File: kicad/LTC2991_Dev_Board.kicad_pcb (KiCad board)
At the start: 2 copper layers, 46.2 x 38.4 mm, 17 parts, among them P1 CONN_01X07, P2 CONN_01X07, Q1 MMBT3904, Q2 MMBT3904, Q3 MMBT3904, Q4 MMBT3904, SW1 DIP-SPDT-3, U1 LTC2991

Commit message: More PCB layout work, schematic tweaks. Closer to a finaly layout.
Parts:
- removed REF**: DIP_switch_2x06, Local:DIP_Switch_2x06
- removed REF**: Pin_Header_Straight_2x03, Pin_Headers:Pin_Header_Straight_2x03
- removed SW1: DIP-SPDT-3, Local:DIP_Switch_2x06
- added P3: CONN_02X03, Pin_Headers:Pin_Header_Straight_2x03, F.Cu at (99.8, 100.3)
- R1, R2, R3, R4: footprint Resistors_SMD:R_2010 -> Resistors_SMD:R_1206
- R5, R6, R7: footprint Resistors_SMD:R_1206 -> Resistors_SMD:R_0603
- moved R7 38.3 mm to (104.9, 92.3), turned to 270 degrees
- moved R6 33.8 mm to (102.4, 92.3), turned to 270 degrees
- moved R5 29.8 mm to (99.8, 92.3), turned to 270 degrees
- moved Q3 13.4 mm to (113.3, 100.2), turned to 180 degrees
- moved Q4 9.79 mm to (113.3, 90.6), turned to 180 degrees
- moved U1 7.37 mm to (102.4, 85.1)
- moved Q2 7.24 mm to (91.3, 100.2), turned to 180 degrees
- moved Q1 7.00 mm to (91.3, 90.6), turned to 180 degrees
- moved R4 1.49 mm to (113.3, 87.2), turned to 0 degrees
- moved R1 1.45 mm to (91.3, 87.2), turned to 0 degrees
- moved R3 0.81 mm to (113.3, 96.9), turned to 0 degrees
- moved R2 0.74 mm to (91.3, 96.9), turned to 0 degrees
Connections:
- R5 pad 2: Net-(R5-Pad2) -> Net-(P3-Pad2)
- R6 pad 2: Net-(R6-Pad2) -> Net-(P3-Pad4)
- R7 pad 2: Net-(R7-Pad2) -> Net-(P3-Pad6)
- U1 pad 13: Net-(SW1-Pad5) -> Net-(P3-Pad6)
- U1 pad 14: Net-(SW1-Pad3) -> Net-(P3-Pad4)
- U1 pad 15: Net-(SW1-Pad1) -> Net-(P3-Pad2)
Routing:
- net Net-(P3-Pad2): track 0.00 -> 18.2 mm, vias 0 -> 2
- net Net-(P3-Pad4): track 0.00 -> 17.2 mm, vias 0 -> 2
- net /V1: track 25.7 -> 9.36 mm
- net Net-(P3-Pad6): track 0.00 -> 16.2 mm
- net /V3: track 22.3 -> 8.14 mm
- net /VCC: track 0.00 -> 14.2 mm
- net /V5: track 5.12 -> 14.1 mm
- net /V7: track 7.94 -> 13.9 mm
- net /V2: track 17.3 -> 13.5 mm
- net /V6: track 7.23 -> 9.51 mm
- net /V4: track 14.4 -> 12.6 mm
- added copper zone on F.Cu, net /GND
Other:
- board size 46.2 x 38.4 mm -> 29.5 x 22 mm
- net class Default: trace_width 0.3048 -> 0.254; via_dia 0.6 -> 0.508; via_drill 0.4 -> 0.3302
- net class Power: clearance 0.3048 -> 0.2032; via_dia 0.6 -> 0.762; via_drill 0.4 -> 0.508
- rule trace_min: 0.2 -> 0.1524
- rule via_min_drill: 0.3 -> 0.3302
- rule via_min_size: 0.4 -> 0.508

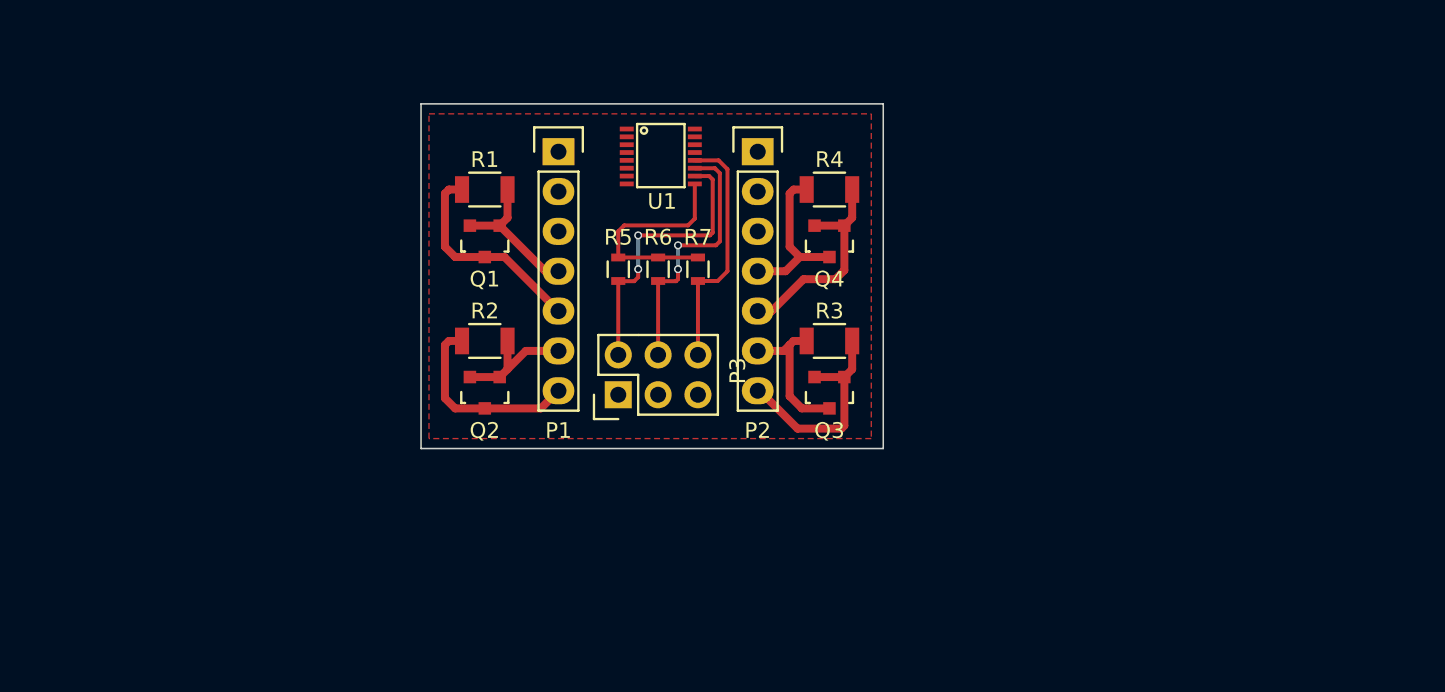
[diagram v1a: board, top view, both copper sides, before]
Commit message: Final schematic and PCB layout for Rev. A. Significantly simplified the schematic in order to make the board as compact as possible.
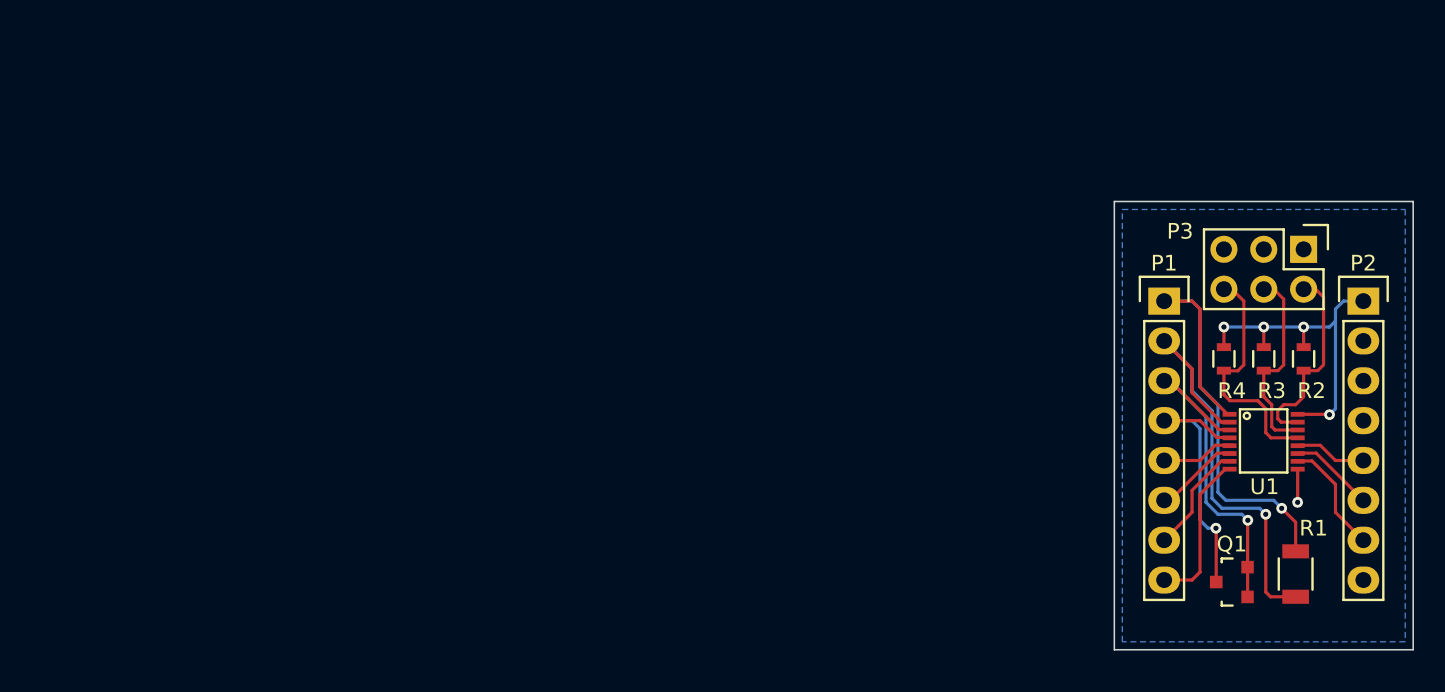
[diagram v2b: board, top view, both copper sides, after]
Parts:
- removed Q2, Q3, Q4: MMBT3904, Housings_SOT-23_SOT-143_TSOT-6:SOT-23
- removed R5, R6, R7: 5k6, Resistors_SMD:R_0603
- P1, P2: value CONN_01X07 -> CONN_01X08; footprint Pin_Headers:Pin_Header_Straight_1x07 -> Pin_Headers:Pin_Header_Straight_1x08
- R2, R3, R4: value 0.1 -> 5k6; footprint Resistors_SMD:R_1206 -> Resistors_SMD:R_0603
- moved R1 57.2 mm to (143.0, 111.8), turned to 90 degrees
- moved Q1 52.3 mm to (138.9, 112.3), turned to 90 degrees
- moved R2 52.2 mm to (143.5, 98.0), turned to 270 degrees
- moved P3 44.7 mm to (143.5, 91.1), turned to 270 degrees
- moved U1 42.7 mm to (141.0, 103.3)
- moved P1 39.8 mm to (134.6, 94.4)
- moved P2 39.8 mm to (147.3, 94.4)
- moved R3 27.7 mm to (141.0, 98.0), turned to 270 degrees
- moved R4 27.4 mm to (138.4, 98.0), turned to 270 degrees
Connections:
- P1 pad 1: /VCC -> /V1
- P1 pad 2: /SCL -> /V2
- P1 pad 3: /SDA -> /V3
- P1 pad 4: /V1 -> /V4
- P1 pad 5: /V2 -> /V5
- P1 pad 6: /V3 -> /V6
- P1 pad 7: /V4 -> /V7
- P2 pad 1: /GND -> /VCC
- P2 pad 2: /PWM -> /GND
- P2 pad 4: /V8 -> /GND
- P2 pad 5: /V7 -> /PWM
- P2 pad 6: /V6 -> /SCL
- P2 pad 7: /V5 -> /SDA
- Q1 pad 1: /V1 -> /V3
- Q1 pad 2: /V1 -> /V3
- Q1 pad 3: /V2 -> /V4
- R2 pad 1: /V4 -> /VCC
- R2 pad 2: /V3 -> Net-(P3-Pad2)
- R3 pad 1: /V6 -> /VCC
- R3 pad 2: /V5 -> Net-(P3-Pad4)
- R4 pad 1: /V8 -> /VCC
- R4 pad 2: /V7 -> Net-(P3-Pad6)
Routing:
- net /V1: track 9.36 -> 32.3 mm, vias 0 -> 1
- net /V2: track 13.5 -> 29.3 mm, vias 0 -> 1
- net /V3: track 8.14 -> 22.4 mm, vias 0 -> 1
- net /V5: track 14.1 -> 4.75 mm
- net /VCC: track 14.2 -> 22.0 mm, vias 0 -> 4
- net /SDA: track 0.00 -> 7.14 mm
- net /V7: track 13.9 -> 7.26 mm
- net Net-(P3-Pad2): track 18.2 -> 12.8 mm, vias 2 -> 0
- net /SCL: track 0.00 -> 5.26 mm
- net /V4: track 12.6 -> 17.8 mm, vias 0 -> 1
- net Net-(P3-Pad4): track 17.2 -> 12.7 mm, vias 2 -> 0
- net /PWM: track 0.00 -> 4.41 mm
- net /V6: track 9.51 -> 5.60 mm
- net /GND: track 0.46 -> 2.11 mm, vias 0 -> 1
- net Net-(P3-Pad6): track 16.2 -> 15.4 mm
- added copper zone on B.Cu, net /GND
- removed copper zone on F.Cu, net /GND
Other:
- board size 29.5 x 22 mm -> 19.1 x 28.6 mm
- net class Default: clearance 0.2032 -> 0.1524; trace_width 0.254 -> 0.2032; via_dia 0.508 -> 0.6858
- net class Power removed
- rule trace_clearance: 0.2032 -> 0.1524
- rule via_min_size: 0.508 -> 0.6858
- board text added: "LTC2991 Dev Board Rev. A, July 2015 http://www.nellump.net/"

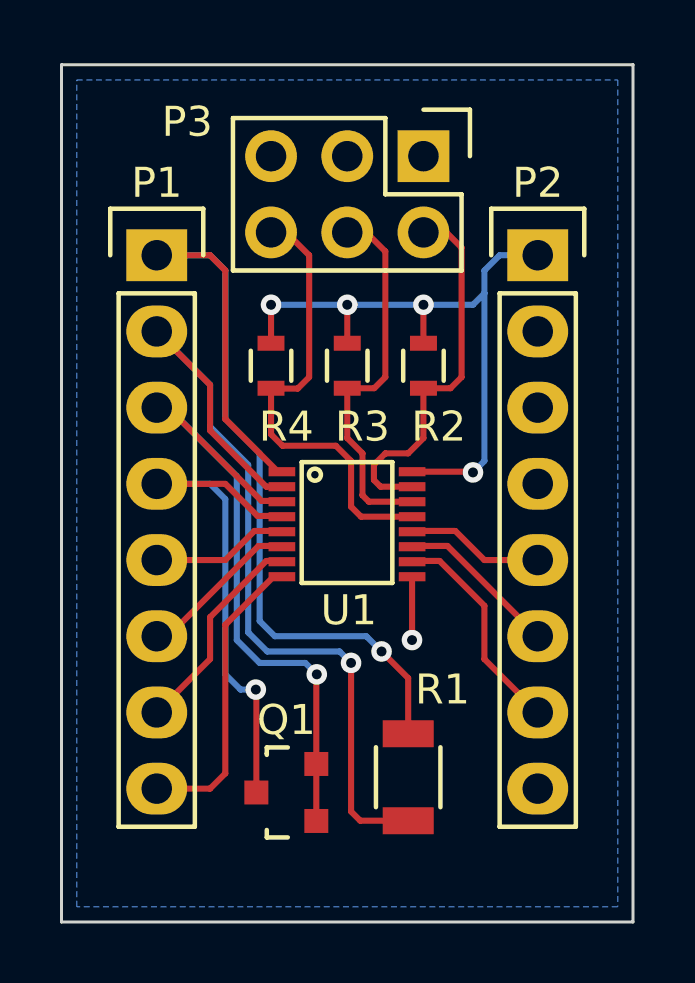
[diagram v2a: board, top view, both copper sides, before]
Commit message: Minor adjustment to PCB silkscreen. Added labels to pins in address jumper. Moved board name to front side.
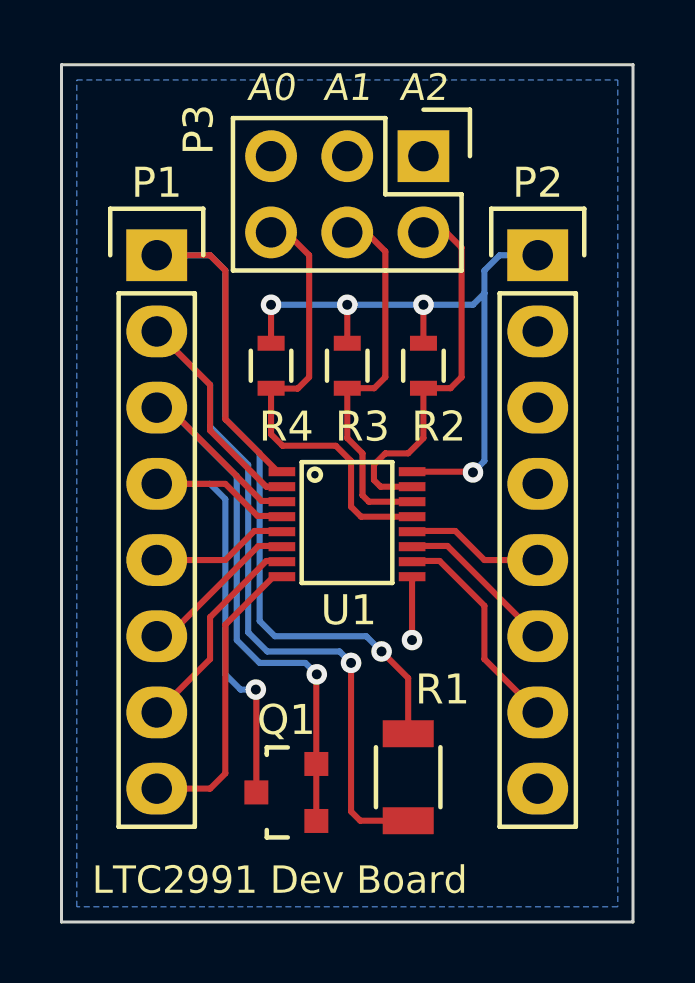
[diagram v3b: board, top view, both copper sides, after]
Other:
- board text added: "A0"
- board text added: "A1"
- board text added: "A2"
- board text added: "LTC2991 Dev Board"
- board text added: "Rev. A, July 2015 http://www.nellump.net/"
- board text removed: "LTC2991 Dev Board Rev. A, July 2015 http://www.nellump.net/"
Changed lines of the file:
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@@
     (links 33)
     (no_connects 0)
-    (area 129.559267 87.960999 152.380734 116.636001)
+    (area 129.559267 87.9221 152.380734 116.636001)
     (thickness 1.6)
-    (drawings 5)
+    (drawings 9)
     (tracks 135)
     (zones 0)
@@
     (descr "Through hole pin header")
     (tags "pin header")
-    (fp_text reference P3 (at -1.143 7.874 360) (layer F.SilkS)
+    (fp_text reference P3 (at -0.889 7.493 450) (layer F.SilkS)
       (effects (font (size 1 1) (thickness 0.15)))
     )
@@
       (net 1 /VCC))
   )
-  (gr_text "LTC2991 Dev Board\nRev. A, July 2015\nhttp://www.nellump.net/" (at 140.97 96.774 90) (layer B.SilkS)
+  (gr_text "LTC2991 Dev Board" (at 132.461 115.189) (layer F.SilkS)
+    (effects (font (size 0.9144 0.9144) (thickness 0.1524)) (justify left))
+  )
+  (gr_text A2 (at 143.51 88.773) (layer F.SilkS)
+    (effects (font (size 0.889 0.889) (thickness 0.1524) italic))
+  )
+  (gr_text A1 (at 140.97 88.773) (layer F.SilkS)
+    (effects (font (size 0.889 0.889) (thickness 0.1524) italic))
+  )
+  (gr_text A0 (at 138.43 88.773) (layer F.SilkS)
+    (effects (font (size 0.889 0.889) (thickness 0.1524) italic))
+  )
+  (gr_text "Rev. A, July 2015\nhttp://www.nellump.net/" (at 140.97 96.139 90) (layer B.SilkS)
     (effects (font (size 1.016 1.016) (thickness 0.254)) (justify left mirror))
   )

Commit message: Minor adjustments to text on PCB's back silkscreen.
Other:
- board text added: "Rev. A, July 2015 http://www.nellump.net/ltcdev"
- board text removed: "Rev. A, July 2015 http://www.nellump.net/"
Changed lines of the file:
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@@
   (title_block
     (title "LTC2991 Development Board")
-    (date 2015-07-15)
+    (date 2015-07-17)
     (rev A)
     (company "Paul Mullen <pm@nellump.net>")
@@
     (visible_elements FFFFF77F)
     (pcbplotparams
-      (layerselection 0x010f0_80000001)
+      (layerselection 0x010f8_80000001)
       (usegerberextensions false)
       (excludeedgelayer true)
@@
       (drillshape 0)
       (scaleselection 1)
-      (outputdirectory ""))
+      (outputdirectory ../gerbers/))
   )
   (net 0 "")
@@
     (effects (font (size 0.889 0.889) (thickness 0.1524) italic))
   )
-  (gr_text "Rev. A, July 2015\nhttp://www.nellump.net/" (at 140.97 96.139 90) (layer B.SilkS)
-    (effects (font (size 1.016 1.016) (thickness 0.254)) (justify left mirror))
+  (gr_text "Rev. A, July 2015\nhttp://www.nellump.net/ltcdev" (at 140.97 94.996 90) (layer B.SilkS)
+    (effects (font (size 1.016 0.889) (thickness 0.1905)) (justify left mirror))
   )
   (gr_line (start 131.445 116.586) (end 131.445 88.011) (angle 90) (layer Edge.Cuts) (width 0.1))

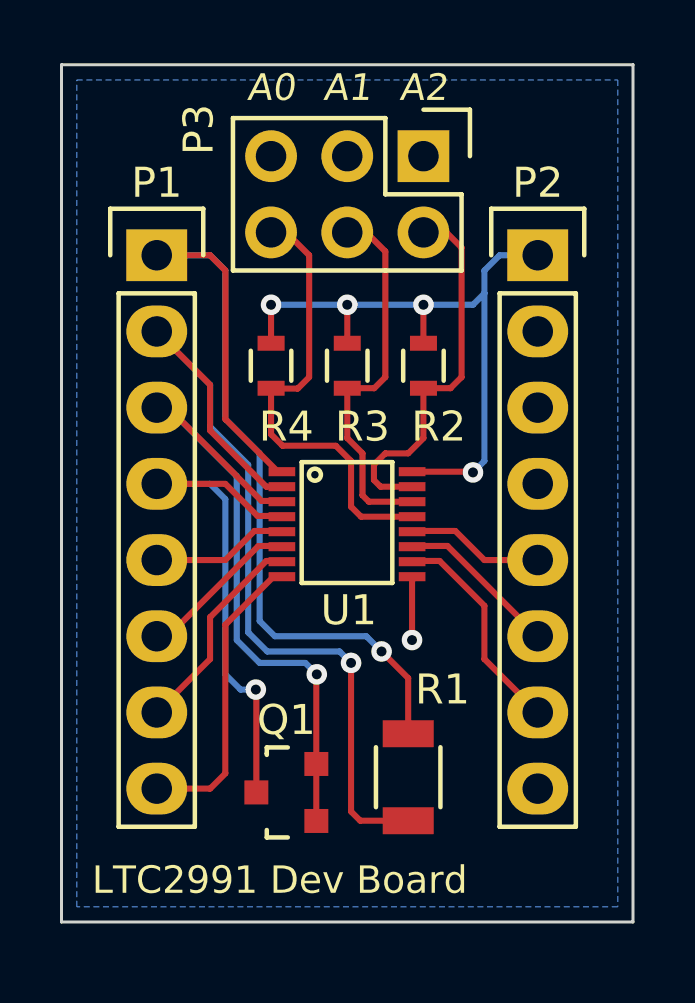
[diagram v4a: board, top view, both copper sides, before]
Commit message: Modified schematic and PCB layout. 1. Added two-pin header for measurement of external current source via    on-board shunt resistor (both optional). 2. Added filter capacitor for IC power. 3. Added filter capacitor for temperature-sensing transistor (both    optional). 4. Placed noise-shielding traces around temperature-sensing    transistor.
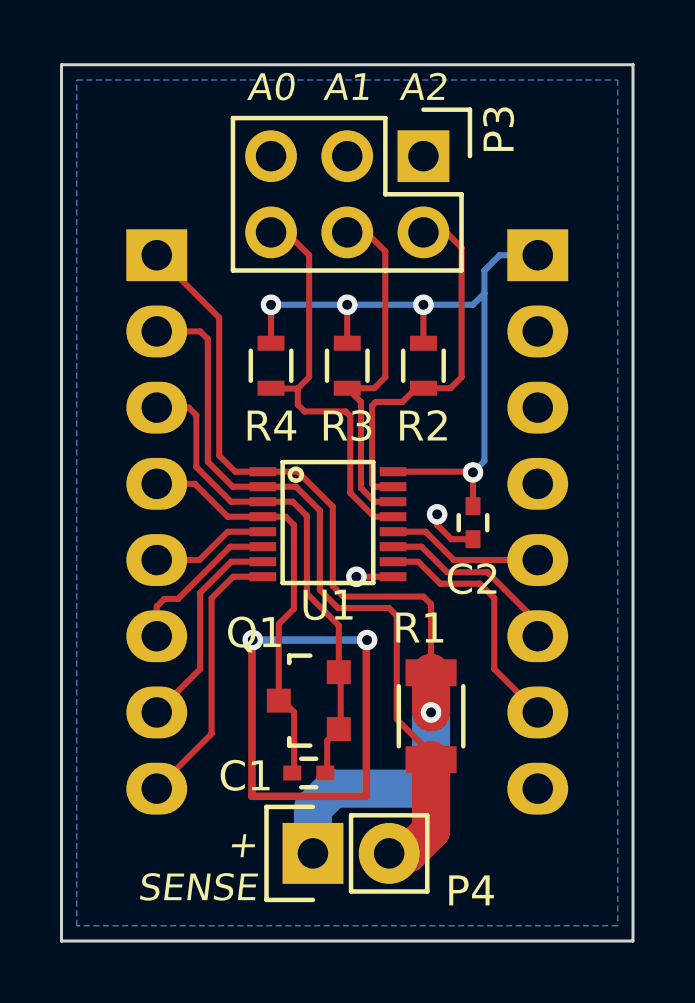
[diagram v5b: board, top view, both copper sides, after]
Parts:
- added C1: 470p, Capacitors_SMD:C_0402, F.Cu at (139.7, 111.6)
- added C2: 0.1μ, Capacitors_SMD:C_0402, F.Cu at (145.2, 103.3)
- added P4: CONN_SENSE, Pin_Headers:Pin_Header_Straight_1x02, F.Cu at (139.8, 114.3)
- P1, P2: moved to B.Cu
- moved Q1 3.15 mm to (139.7, 109.2)
- moved R1 2.17 mm to (143.8, 109.7), turned to 270 degrees
- moved U1 0.63 mm to (140.3, 103.3)
- turned P1 to 180 degrees
- turned P2 to 180 degrees
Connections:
- P2 pad 2: /GND -> /NC
- P2 pad 3: /GND -> /NC
- P2 pad 4: /GND -> /NC
- R1 pad 1: /V2 -> /V1
- R1 pad 2: /V1 -> /V2
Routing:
- net (no net): track 0.00 -> 18.0 mm, vias 0 -> 2
- net /V3: track 22.4 -> 16.7 mm, vias 1 -> 0
- net /V2: track 29.3 -> 25.2 mm, vias 1 -> 0
- net /V4: track 17.8 -> 13.8 mm, vias 1 -> 0
- net /V1: track 32.3 -> 30.0 mm
- net /VCC: track 22.0 -> 23.8 mm
- net Net-(P3-Pad6): track 15.4 -> 13.9 mm
- net /SDA: track 7.14 -> 8.29 mm
- net /V8: track 10.2 -> 9.11 mm
- net /SCL: track 5.26 -> 6.33 mm
- net /GND: track 2.11 -> 2.98 mm, vias 1 -> 2
- net /V5: track 4.75 -> 3.93 mm
- net /PWM: track 4.41 -> 5.21 mm
- net Net-(P3-Pad4): track 12.7 -> 11.9 mm
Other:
- board size 19.1 x 28.6 mm -> 19.1 x 29.2 mm
- board text added: "+ SENSE"
- board text added: "LTC2991 Dev Board Rev. B, July 2015 http://www.nellump.net/ltcdev"
- board text removed: "LTC2991 Dev Board"
- board text removed: "Rev. A, July 2015 http://www.nellump.net/ltcdev"

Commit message: Rearranged schematic. In the hopes of making it a bit more readable. Updated PCB layout with new netlist (no significant changes).
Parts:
- P1, P2: value CONN_01X08 -> PIN_HEAD_1x8
- P3: value CONN_02X03 -> PIN_HEAD_2x3
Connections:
- net Net-(P3-Pad2) renamed /ADR2
- net Net-(P3-Pad4) renamed /ADR1
- net Net-(P3-Pad6) renamed /ADR0
